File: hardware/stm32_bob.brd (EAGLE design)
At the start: 160 x 100 mm, 52 parts, among them U1 F3_DISCOVERY, U2 LSF0108, U3 INA827, U4 INA827

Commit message: Added values for populated components
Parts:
- added C3, C4: .1u, rcl:C0805
- C1, C2: value (none) -> .1u
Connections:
- net 3V: now also C4.1
- net 5V: now also C3.1
- net GND: now also C3.2, C4.2
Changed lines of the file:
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@@
 <element name="R3" library="rcl" package="R1206" value="0R" x="-31.75" y="-45.72"/>
 <element name="R4" library="rcl" package="R1206" value="0R" x="-31.75" y="-50.8"/>
-<element name="C1" library="rcl" package="C0805" value="" x="-33.02" y="-55.88"/>
-<element name="C2" library="rcl" package="C0805" value="" x="-33.02" y="-60.96"/>
+<element name="C1" library="rcl" package="C0805" value=".1u" x="-33.02" y="-55.88"/>
+<element name="C2" library="rcl" package="C0805" value=".1u" x="-33.02" y="-60.96"/>
 <element name="REF_SEL" library="SparkFun-Connectors" package="1X03" value="" x="-33.02" y="-66.04"/>
 <element name="LVL_EN" library="SparkFun-Connectors" package="1X02" value="M02PTH" x="-33.02" y="-71.12"/>
@@
 <element name="R28" library="rcl" package="R0805" value="330" x="-88.9" y="-222.25"/>
 <element name="R29" library="rcl" package="R0805" value="330" x="-88.9" y="-228.6"/>
+<element name="C3" library="rcl" package="C0805" value=".1u" x="-88.9" y="-234.95"/>
+<element name="C4" library="rcl" package="C0805" value=".1u" x="-88.9" y="-241.3"/>
 </elements>
 <signals>
@@
 <contactref element="PB4" pad="C1"/>
 <contactref element="PB4" pad="C2"/>
+<contactref element="C4" pad="2"/>
+<contactref element="C3" pad="2"/>
 <wire x1="-78.97" y1="-158.79" x2="-90.17" y2="-158.79" width="0" layer="19" extent="1-1"/>
 <wire x1="-76.2" y1="-158.79" x2="-78.97" y2="-158.79" width="0" layer="19" extent="1-1"/>
@@
 <wire x1="-37.06" y1="-158.79" x2="-48.26" y2="-158.79" width="0" layer="19" extent="1-1"/>
 <wire x1="-33.02" y1="-165.1" x2="-37.06" y2="-158.79" width="0" layer="19" extent="1-1"/>
+<wire x1="-87.95" y1="-234.95" x2="-90.17" y2="-158.79" width="0" layer="19" extent="1-1"/>
+<wire x1="-87.95" y1="-241.3" x2="-87.95" y2="-234.95" width="0" layer="19" extent="1-1"/>
 <wire x1="-33.02" y1="-71.12" x2="-37.06" y2="-158.79" width="0" layer="19" extent="1-1"/>
 <wire x1="-33.02" y1="-66.04" x2="-33.02" y2="-71.12" width="0" layer="19" extent="1-1"/>
@@
 <contactref element="R28" pad="1"/>
 <contactref element="R29" pad="1"/>
+<contactref element="C4" pad="1"/>
 <wire x1="-33.97" y1="-114.3" x2="-33.97" y2="-119.38" width="0" layer="19" extent="1-1"/>
 <wire x1="-33.97" y1="-109.22" x2="-33.97" y2="-114.3" width="0" layer="19" extent="1-1"/>
@@
 <wire x1="-89.85" y1="-222.25" x2="-89.85" y2="-215.9" width="0" layer="19" extent="1-1"/>
 <wire x1="-89.85" y1="-228.6" x2="-89.85" y2="-222.25" width="0" layer="19" extent="1-1"/>
+<wire x1="-89.85" y1="-241.3" x2="-89.85" y2="-228.6" width="0" layer="19" extent="1-1"/>
 <wire x1="-33.64" y1="5.08" x2="-32.07" y2="-83.82" width="0" layer="19" extent="1-1"/>
 <wire x1="6.35" y1="5.08" x2="-33.64" y2="5.08" width="0" layer="19" extent="1-1"/>
@@
 <contactref element="R20" pad="1"/>
 <contactref element="R21" pad="1"/>
+<contactref element="C3" pad="1"/>
 <wire x1="-33.97" y1="-154.94" x2="-33.97" y2="-160.02" width="0" layer="19" extent="1-1"/>
 <wire x1="-33.97" y1="-149.86" x2="-33.97" y2="-154.94" width="0" layer="19" extent="1-1"/>
@@
 <wire x1="6.35" y1="91.44" x2="6.35" y2="88.9" width="0" layer="19" extent="1-1"/>
 <wire x1="81.28" y1="91.44" x2="6.35" y2="91.44" width="0" layer="19" extent="1-1"/>
+<wire x1="-89.85" y1="-234.95" x2="-33.97" y2="-160.02" width="0" layer="19" extent="1-1"/>
 </signal>
 <signal name="PF9">

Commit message: oops forgot one
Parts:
- R5: value (none) -> 200k
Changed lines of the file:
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@@
 <element name="REF_SEL" library="SparkFun-Connectors" package="1X03" value="" x="-33.02" y="-66.04"/>
 <element name="LVL_EN" library="SparkFun-Connectors" package="1X02" value="M02PTH" x="-33.02" y="-71.12"/>
-<element name="R5" library="rcl" package="R0805" value="" x="-33.02" y="-78.74"/>
+<element name="R5" library="rcl" package="R0805" value="200k" x="-33.02" y="-78.74"/>
 <element name="R6" library="rcl" package="R0805" value="" x="-33.02" y="-83.82"/>
 <element name="R7" library="rcl" package="R0805" value="" x="-33.02" y="-88.9"/>

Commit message: Fully routed board
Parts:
- moved R26 341.1 mm to (91.4, 80.0)
- moved C4 339.1 mm to (57.1, 64.8), turned to 90 degrees
- moved C3 336.8 mm to (64.8, 64.8), turned to 90 degrees
- moved R27 335.8 mm to (91.4, 67.3)
- moved R28 330.4 mm to (91.4, 54.6)
- moved LED1 325.1 mm to (91.4, 77.5), turned to 180 degrees
- moved R29 324.1 mm to (91.4, 40.6)
- moved LED2 317.8 mm to (91.4, 64.8), turned to 180 degrees
- moved LED3 310.5 mm to (91.4, 52.1), turned to 180 degrees
- moved LED4 302.3 mm to (91.4, 38.1), turned to 180 degrees
- moved R22 298.1 mm to (71.1, 78.7), turned to 90 degrees
- moved R23 291.7 mm to (71.1, 66.0), turned to 90 degrees
- moved R24 285.3 mm to (71.1, 53.3), turned to 90 degrees
- moved R25 278.0 mm to (71.1, 39.4), turned to 90 degrees
- moved R21 276.0 mm to (91.4, 86.4), turned to 90 degrees
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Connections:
- removed net PF5: JP2.12
- net 5V: no longer C3.1
- net PE5: now also JP2.12
- net VDD_B: now also C3.1
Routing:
- net GND: track 0.00 -> 359.7 mm, vias 0 -> 17
- net 3V: track 0.00 -> 254.3 mm, vias 0 -> 6
- net 5V: track 0.00 -> 220.7 mm, vias 0 -> 6
- net PE13: track 0.00 -> 107.9 mm, vias 0 -> 7
- net PD7: track 0.00 -> 90.7 mm, vias 0 -> 3
- net PA0: track 0.00 -> 85.4 mm
- net PD11: track 0.00 -> 84.1 mm, vias 0 -> 4
- net PD10: track 0.00 -> 81.9 mm, vias 0 -> 3
- net PD5: track 0.00 -> 80.4 mm, vias 0 -> 2
- net PD2: track 0.00 -> 76.8 mm, vias 0 -> 4
- net PE14: track 0.00 -> 76.7 mm, vias 0 -> 1
- net PD6: track 0.00 -> 74.9 mm, vias 0 -> 3
- net PE9: track 0.00 -> 74.6 mm, vias 0 -> 2
- net PA14: track 0.00 -> 73.7 mm, vias 0 -> 1
- net PD0: track 0.00 -> 73.2 mm, vias 0 -> 4
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- added copper zone on layer 1, net GND
- added copper zone on layer 16, net GND
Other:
- board size 160 x 100 mm -> 103.9 x 97.5 mm
- board text added: "EXT"
- board text added: "GND"

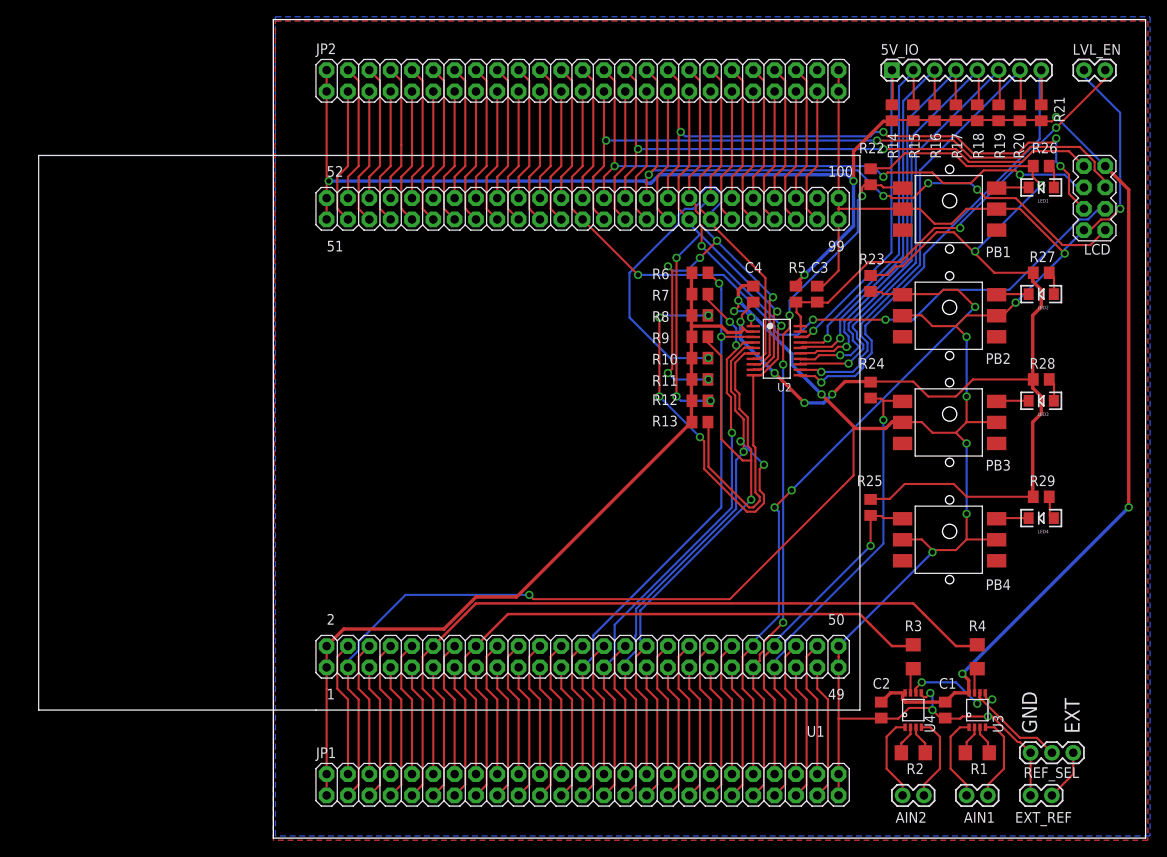
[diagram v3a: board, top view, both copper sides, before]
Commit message: Added version 2 of board using 40 pin header
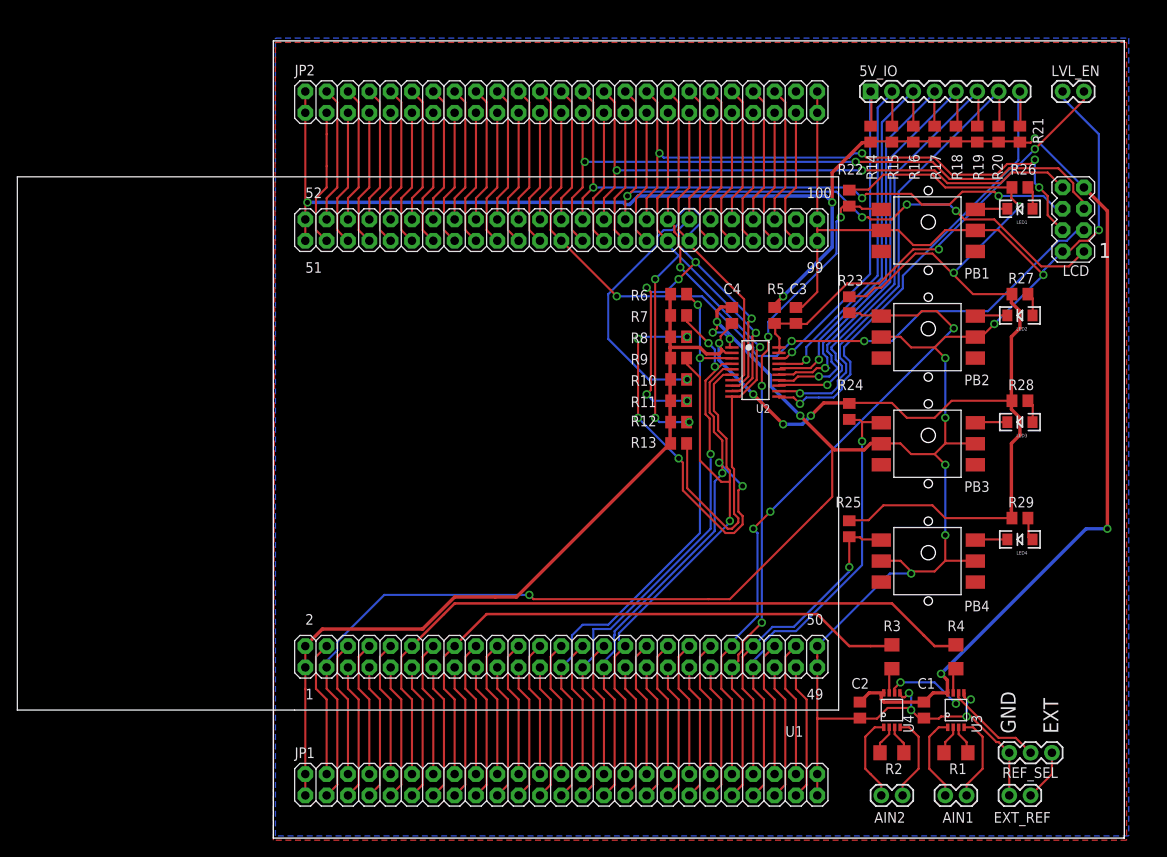
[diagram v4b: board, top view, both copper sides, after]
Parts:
- moved LCD 3.59 mm to (95.2, 73.7)
- moved PB1 3.59 mm to (72.4, 69.8)
- moved R15 3.59 mm to (73.7, 83.8)
- moved R17 3.59 mm to (78.7, 83.8)
- moved R19 3.59 mm to (83.8, 83.8)
- moved R20 3.59 mm to (86.4, 83.8)
- moved R23 3.59 mm to (68.6, 63.5)
- moved R24 3.59 mm to (68.6, 50.8)
- moved PB4 3.59 mm to (72.4, 30.5)
- moved JP2 3.59 mm to (3.81, 86.4)
- moved PB2 3.59 mm to (72.4, 57.1)
- moved PB3 3.59 mm to (72.4, 44.5)
- moved R25 3.59 mm to (68.6, 36.8)
- moved R6 3.59 mm to (48.3, 64.8)
- moved C3 3.59 mm to (62.2, 62.2)
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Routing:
- net PD11: track 84.1 -> 81.5 mm
- net PD10: track 81.9 -> 79.3 mm
- net PE14: track 76.7 -> 74.2 mm
- net PE13: track 107.9 -> 105.5 mm
- net GND: track 359.7 -> 357.6 mm
- net PE11: track 71.4 -> 70.2 mm
- net 5V: track 220.7 -> 219.6 mm
- net PD13: track 57.5 -> 56.4 mm
- net 3V: track 254.3 -> 253.3 mm
- net PE9: track 74.6 -> 73.9 mm
- net PD12: track 40.6 -> 40.1 mm
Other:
- board size 103.9 x 97.5 mm -> 101.3 x 94.9 mm
- board text added: "1"
